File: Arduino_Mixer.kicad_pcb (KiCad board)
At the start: 2 copper layers, 142.5 x 99.3 mm, 12 parts

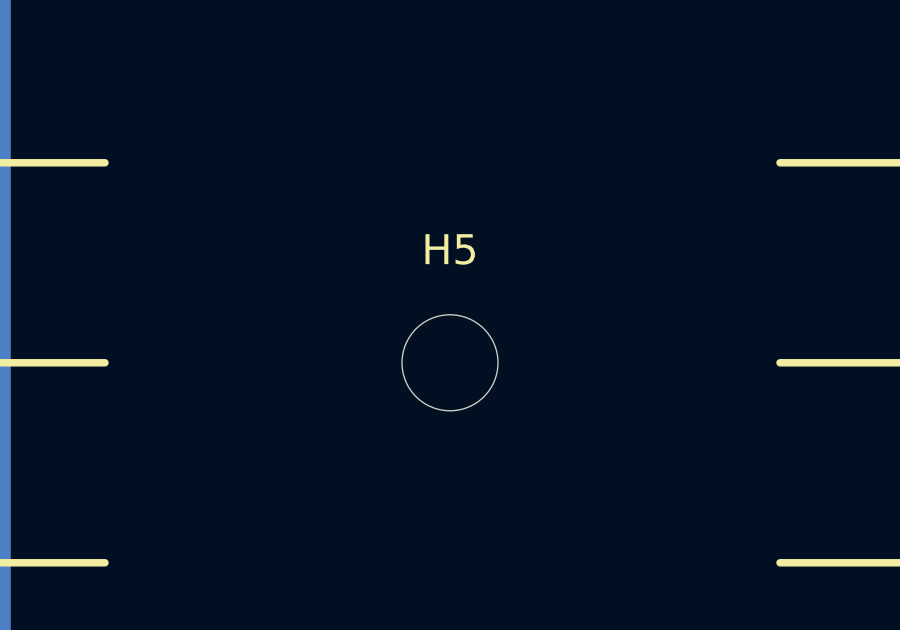
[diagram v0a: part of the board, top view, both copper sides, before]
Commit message: Removed central hole as assymetry would not have worked with assembled PCB when flipped
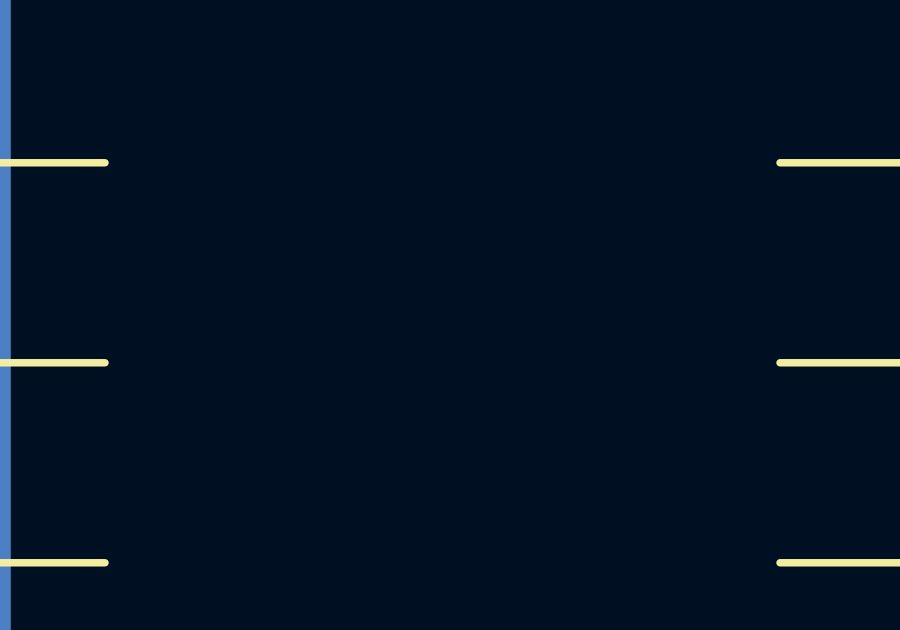
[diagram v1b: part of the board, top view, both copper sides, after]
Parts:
- removed H5: MountingHole, MountingHole:MountingHole_3.2mm_M3_ISO14580
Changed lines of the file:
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@@
 			)
 		)
+		(property ki_fp_filters "MountingHole*")
+		(sheetname "Root")
+		(sheetfile "Arduino_Mixer.kicad_sch")
 		(attr exclude_from_pos_files)
 		(fp_circle
@@
 			)
 		)
+		(property ki_fp_filters "MountingHole*")
+		(sheetname "Root")
+		(sheetfile "Arduino_Mixer.kicad_sch")
 		(attr exclude_from_pos_files)
 		(fp_circle
@@
 			)
 		)
-		(attr exclude_from_pos_files)
-		(fp_circle
-			(center 0 0)
-			(end 2.75 0)
-			(stroke
-				(width 0.15)
-				(type solid)
-			)
-			(fill none)
-			(layer "Cmts.User")
-		)
-		(fp_circle
-			(center 0 0)
-			(end 3 0)
-			(stroke
-				(width 0.05)
-				(type solid)
-			)
-			(fill none)
-			(layer "F.CrtYd")
-		)
-		(fp_text user "${REFERENCE}"
-			(at 0 0 0)
-			(layer "F.Fab")
-			(effects
-				(font
-					(size 1 1)
-					(thickness 0.15)
-				)
-			)
-		)
-		(pad "" np_thru_hole circle
-			(at 0 0)
-			(size 3.2 3.2)
-			(drill 3.2)
-			(layers "*.Cu" "*.Mask")
-		)
-	)
-	(footprint "MountingHole:MountingHole_3.2mm_M3_ISO14580"
-		(layer "F.Cu")
-		(at 165 85)
-		(descr "Mounting Hole 3.2mm, no annular, M3, ISO14580")
-		(tags "mounting hole 3.2mm no annular m3 iso14580")
-		(property "Reference" "H5"
-			(at 0 -3.75 0)
-			(layer "F.SilkS")
-			(effects
-				(font
-					(size 1 1)
-					(thickness 0.15)
-				)
-			)
-		)
-		(property "Value" "MountingHole"
-			(at 0 3.75 0)
-			(layer "F.Fab")
-			(effects
-				(font
-					(size 1 1)
-					(thickness 0.15)
-				)
-			)
-		)
-		(property "Footprint" "MountingHole:MountingHole_3.2mm_M3_ISO14580"
-			(at 0 0 0)
-			(unlocked yes)
-			(layer "F.Fab")
-			(hide yes)
-			(effects
-				(font
-					(size 1.27 1.27)
-				)
-			)
-		)
-		(property "Datasheet" ""
-			(at 0 0 0)
-			(unlocked yes)
-			(layer "F.Fab")
-			(hide yes)
-			(effects
-				(font
-					(size 1.27 1.27)
-				)
-			)
-		)
-		(property "Description" "Mounting Hole without connection"
-			(at 0 0 0)
-			(unlocked yes)
-			(layer "F.Fab")
-			(hide yes)
-			(effects
-				(font
-					(size 1.27 1.27)
-				)
-			)
-		)
+		(property ki_fp_filters "MountingHole*")
+		(sheetname "Root")
+		(sheetfile "Arduino_Mixer.kicad_sch")
 		(attr exclude_from_pos_files)
 		(fp_circle
@@
 			)
 		)
+		(property ki_fp_filters "MountingHole*")
+		(sheetname "Root")
+		(sheetfile "Arduino_Mixer.kicad_sch")
 		(attr exclude_from_pos_files)
 		(fp_circle
@@
 			)
 		)
+		(property ki_fp_filters "Arduino*Nano*")
+		(sheetname "Root")
+		(sheetfile "Arduino_Mixer.kicad_sch")
 		(attr through_hole)
 		(fp_line
@@
 			)
 		)
+		(property ki_fp_filters "Potentiometer*")
+		(sheetname "Root")
+		(sheetfile "Arduino_Mixer.kicad_sch")
 		(attr through_hole)
 		(fp_rect
@@
 			)
 		)
+		(property ki_fp_filters "Potentiometer*")
+		(sheetname "Root")
+		(sheetfile "Arduino_Mixer.kicad_sch")
 		(attr through_hole)
 		(fp_rect
@@
 			)
 		)
+		(property ki_fp_filters "Potentiometer*")
+		(sheetname "Root")
+		(sheetfile "Arduino_Mixer.kicad_sch")
 		(attr through_hole)
 		(fp_rect
@@
 			)
 		)
+		(property ki_fp_filters "Potentiometer*")
+		(sheetname "Root")
+		(sheetfile "Arduino_Mixer.kicad_sch")
 		(attr through_hole)
 		(fp_rect
@@
 			)
 		)
+		(property ki_fp_filters "Potentiometer*")
+		(sheetname "Root")
+		(sheetfile "Arduino_Mixer.kicad_sch")
 		(attr through_hole)
 		(fp_rect
@@
 			)
 		)
+		(property ki_fp_filters "Potentiometer*")
+		(sheetname "Root")
+		(sheetfile "Arduino_Mixer.kicad_sch")
 		(attr through_hole)
 		(fp_rect

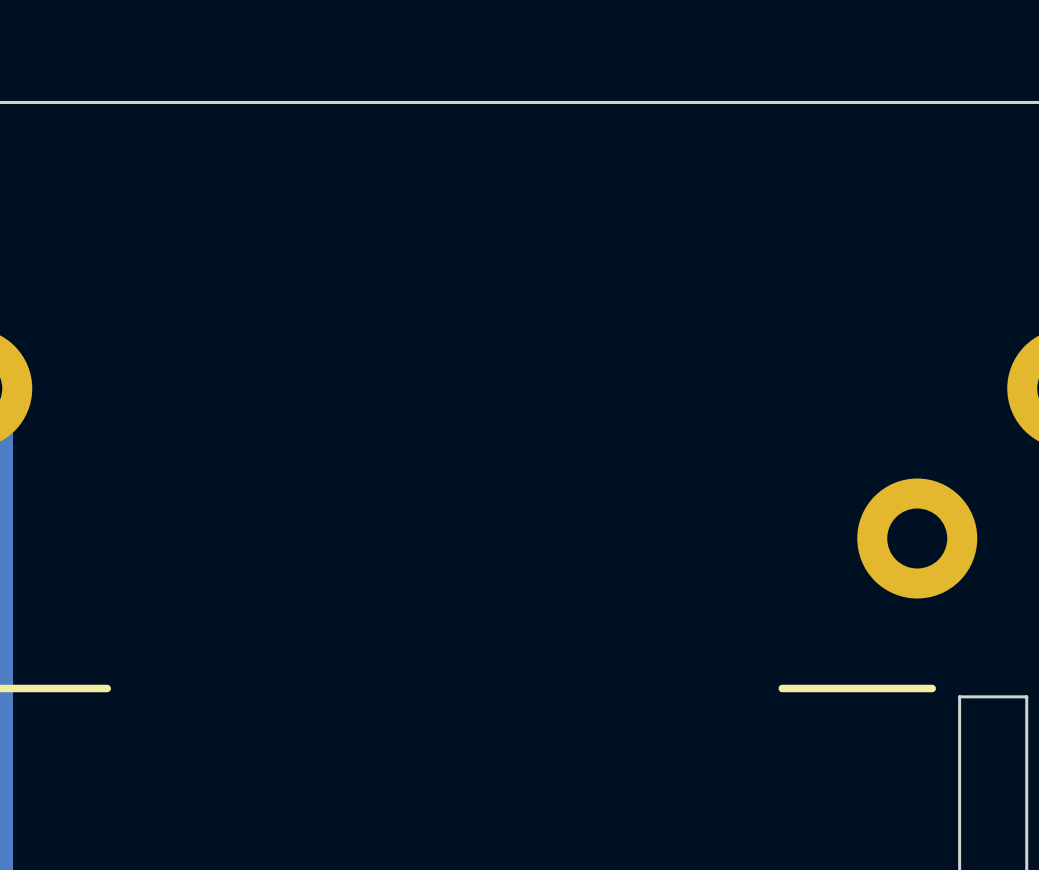
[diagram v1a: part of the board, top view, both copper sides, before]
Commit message: First release candidate Added alw Audio logo, produced gerber plots using JLPCB guidelines: https://jlcpcb.com/help/article/362-how-to-generate-gerber-and-drill-files-in-kicad-8
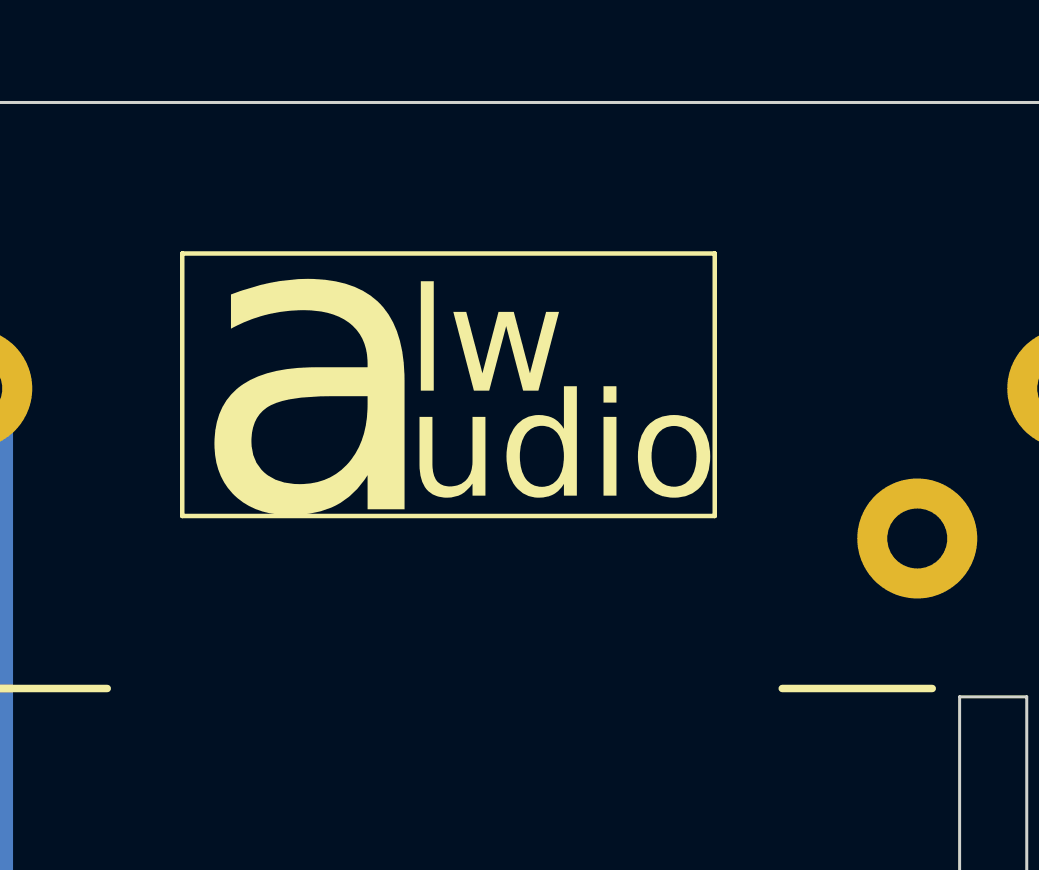
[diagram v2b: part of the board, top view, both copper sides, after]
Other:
- board text added: "a"
- board text added: "lw"
- board text added: "udio"

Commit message: Added JLPCB order number location in bottom silk.
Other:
- board text added: "JLCJLCJLCJLC"
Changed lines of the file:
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@@
 		(layer "Edge.Cuts")
+	)
+	(gr_text "JLCJLCJLCJLC"
+		(at 213 90 90)
+		(layer "B.SilkS")
+		(effects
+			(font
+				(size 1 1)
+				(thickness 0.15)
+			)
+			(justify left bottom mirror)
+		)
 	)
 	(gr_text "udio"

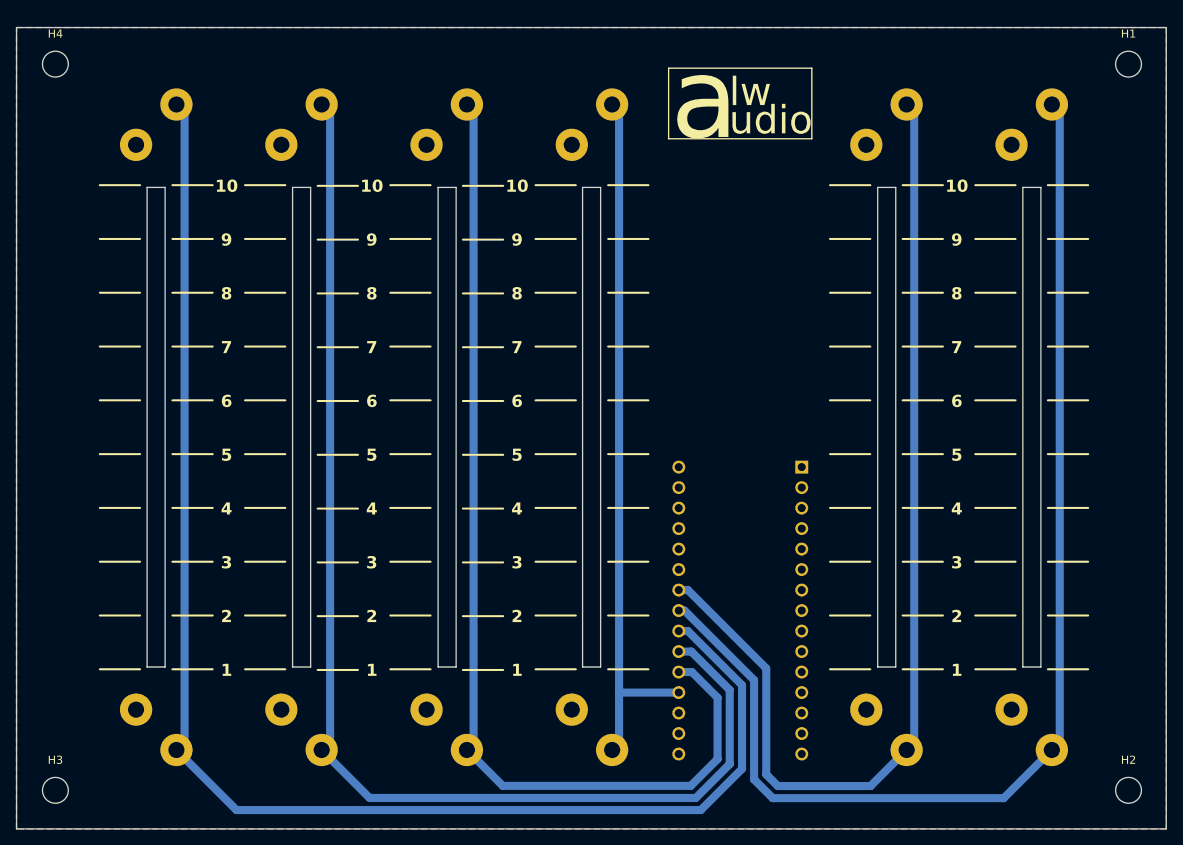
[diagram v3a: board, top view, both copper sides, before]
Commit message: Moved corner hole idents to bottom silk.
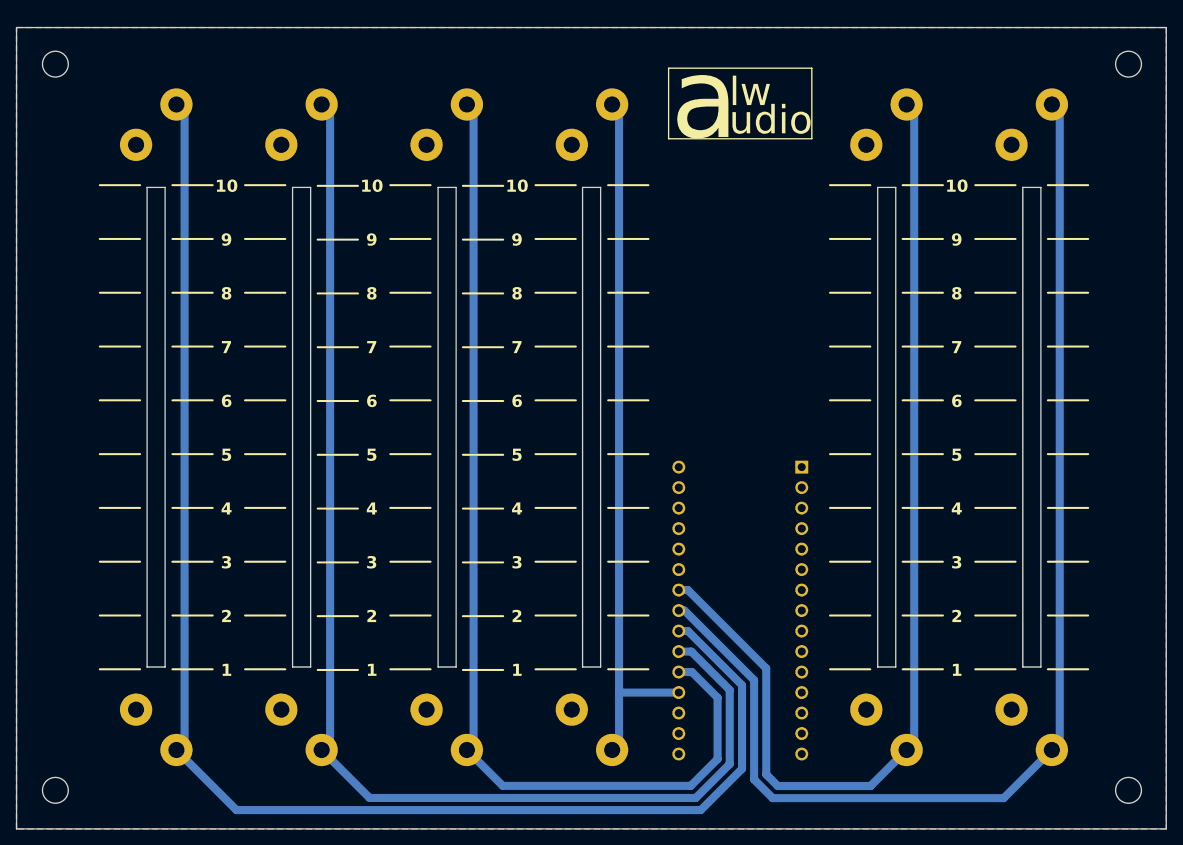
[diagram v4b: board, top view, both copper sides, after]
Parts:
- H1, H2, H3, H4: moved to B.Cu
- turned H1 to 180 degrees
- turned H2 to 180 degrees
- turned H3 to 180 degrees
- turned H4 to 180 degrees
